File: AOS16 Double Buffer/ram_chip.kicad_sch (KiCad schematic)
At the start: 1 part, among them IC3 IS61WV3216BLL-12TLI

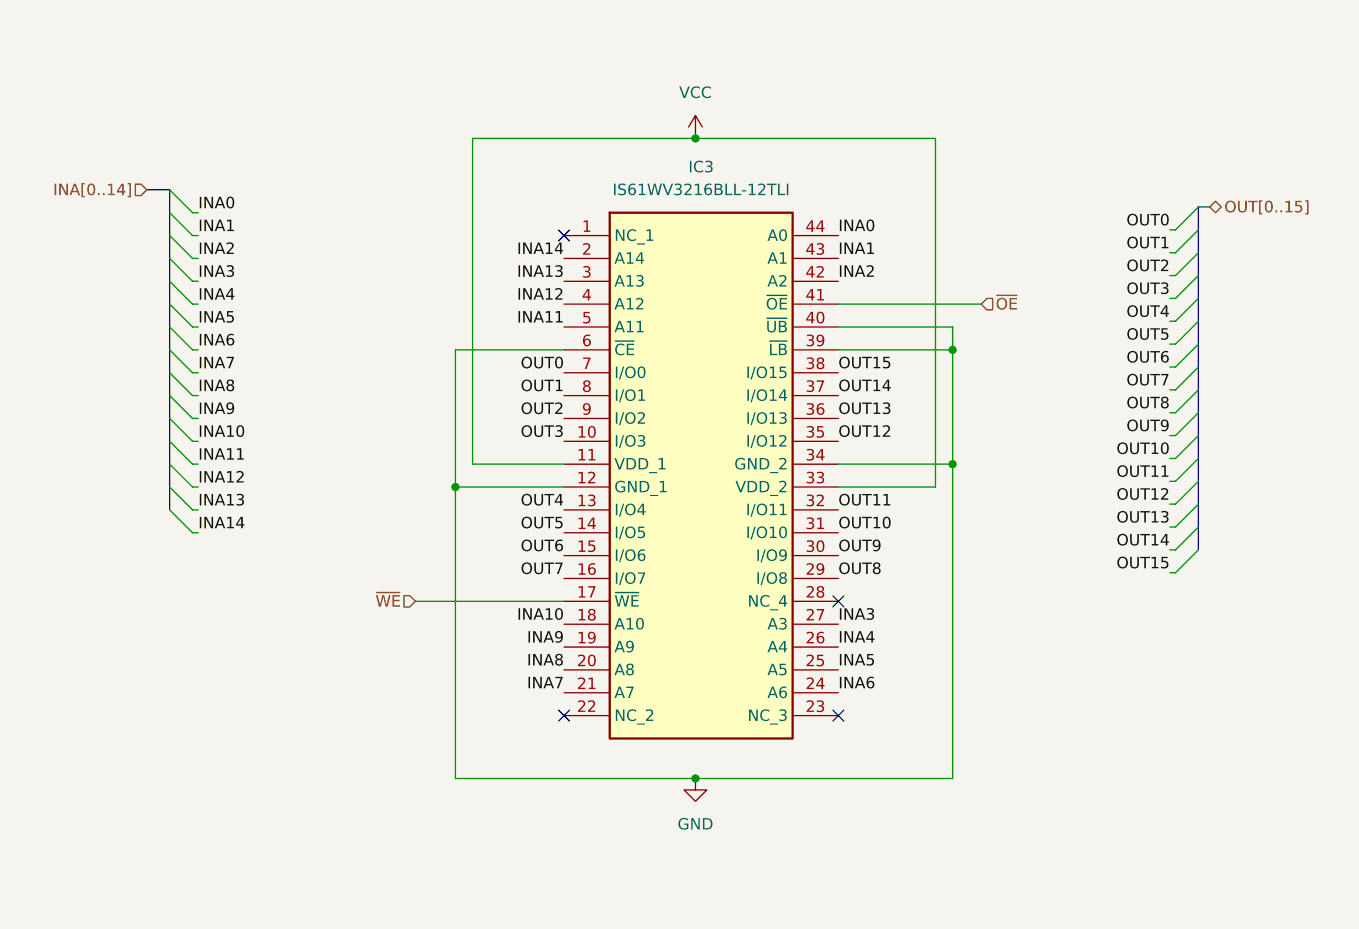
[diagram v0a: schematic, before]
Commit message: updated double buffer
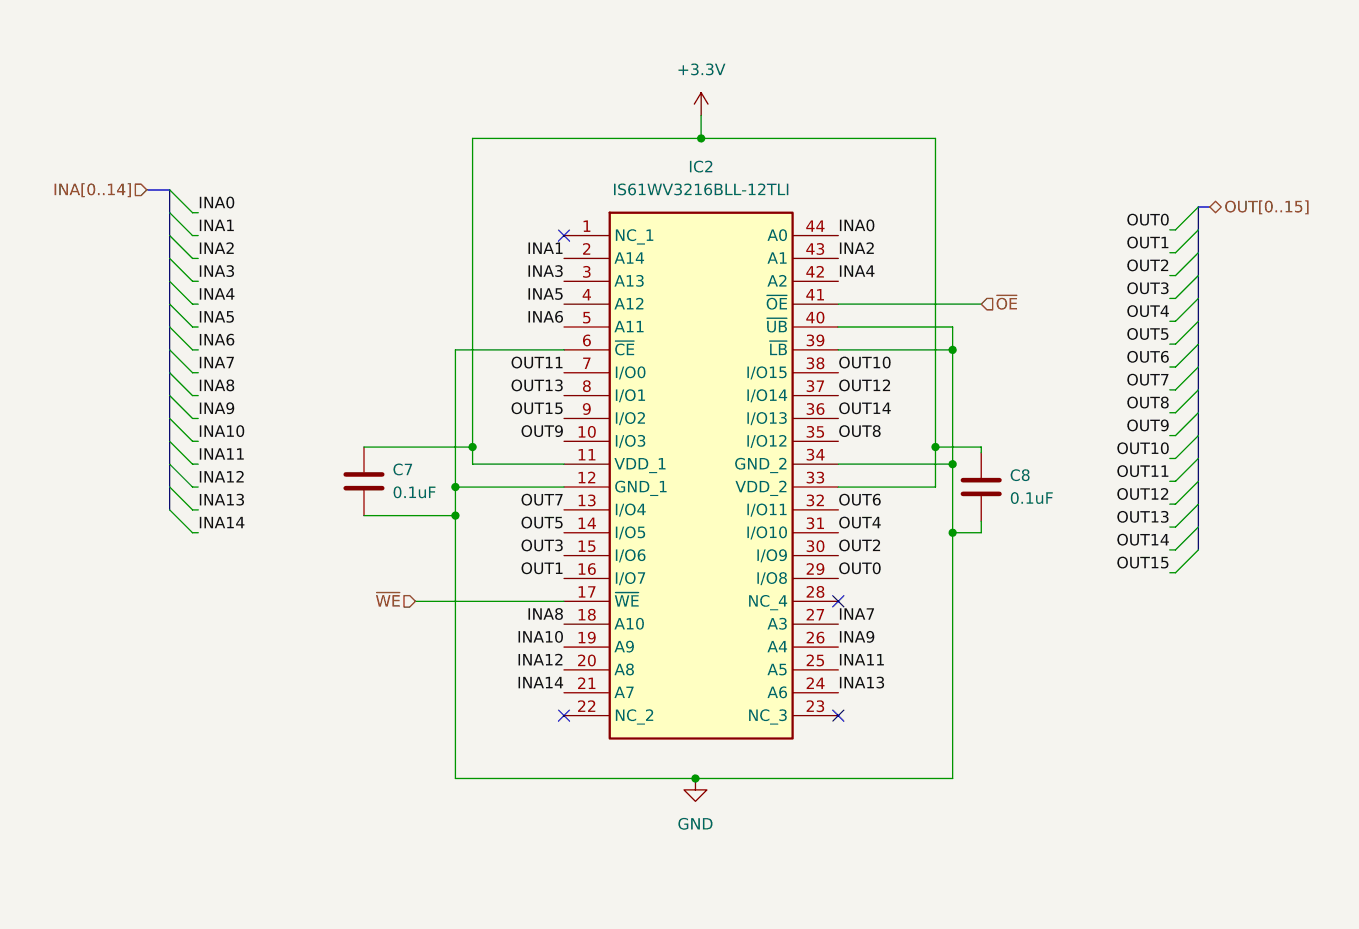
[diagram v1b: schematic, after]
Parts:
- added C7, C8: 0.1uF, Capacitor_SMD:C_0603_1608Metric, symbol Device:C
- renumbered IC3 to IC2
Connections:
- net GND: now also C7.2, C8.2
- net INA1: now also IC2.2 (A14); no longer IC2.43 (A1)
- net INA10: now also IC2.19 (A9); no longer IC2.18 (A10)
- net INA11: now also IC2.25 (A5); no longer IC2.5 (A11)
- net INA12: now also IC2.20 (A8); no longer IC2.4 (A12)
- net INA13: now also IC2.24 (A6); no longer IC2.3 (A13)
- net INA14: now also IC2.21 (A7); no longer IC2.2 (A14)
- net INA2: now also IC2.43 (A1); no longer IC2.42 (A2)
- net INA3: now also IC2.3 (A13); no longer IC2.27 (A3)
- net INA4: now also IC2.42 (A2); no longer IC2.26 (A4)
- net INA5: now also IC2.4 (A12); no longer IC2.25 (A5)
- net INA6: now also IC2.5 (A11); no longer IC2.24 (A6)
- net INA7: now also IC2.27 (A3); no longer IC2.21 (A7)
- net INA8: now also IC2.18 (A10); no longer IC2.20 (A8)
- net INA9: now also IC2.26 (A4); no longer IC2.19 (A9)
- net OUT0: now also IC2.29 (I/O8); no longer IC2.7 (I/O0)
- net OUT1: now also IC2.16 (I/O7); no longer IC2.8 (I/O1)
- net OUT10: now also IC2.38 (I/O15); no longer IC2.31 (I/O10)
- net OUT11: now also IC2.7 (I/O0); no longer IC2.32 (I/O11)
- net OUT12: now also IC2.37 (I/O14); no longer IC2.35 (I/O12)
- net OUT13: now also IC2.8 (I/O1); no longer IC2.36 (I/O13)
- net OUT14: now also IC2.36 (I/O13); no longer IC2.37 (I/O14)
- net OUT15: now also IC2.9 (I/O2); no longer IC2.38 (I/O15)
- net OUT2: now also IC2.30 (I/O9); no longer IC2.9 (I/O2)
- net OUT3: now also IC2.15 (I/O6); no longer IC2.10 (I/O3)
- net OUT4: now also IC2.31 (I/O10); no longer IC2.13 (I/O4)
- net OUT6: now also IC2.32 (I/O11); no longer IC2.15 (I/O6)
- net OUT7: now also IC2.13 (I/O4); no longer IC2.16 (I/O7)
- net OUT8: now also IC2.35 (I/O12); no longer IC2.29 (I/O8)
- net OUT9: now also IC2.10 (I/O3); no longer IC2.30 (I/O9)
- net VCC renamed +3.3V
- net +3.3V: now also C7.1, C8.1

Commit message: Completed double buffer first draft
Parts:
- renumbered C7 to C10, C8 to C11, IC2 to IC1
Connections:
- net OUT0: now also IC1.10 (I/O3); no longer IC1.29 (I/O8)
- net OUT1: now also IC1.36 (I/O13); no longer IC1.16 (I/O7)
- net OUT10: now also IC1.14 (I/O5); no longer IC1.38 (I/O15)
- net OUT11: now also IC1.31 (I/O10); no longer IC1.7 (I/O0)
- net OUT12: now also IC1.15 (I/O6); no longer IC1.37 (I/O14)
- net OUT13: now also IC1.30 (I/O9); no longer IC1.8 (I/O1)
- net OUT14: now also IC1.16 (I/O7); no longer IC1.36 (I/O13)
- net OUT15: now also IC1.29 (I/O8); no longer IC1.9 (I/O2)
- net OUT2: now also IC1.9 (I/O2); no longer IC1.30 (I/O9)
- net OUT3: now also IC1.37 (I/O14); no longer IC1.15 (I/O6)
- net OUT4: now also IC1.8 (I/O1); no longer IC1.31 (I/O10)
- net OUT5: now also IC1.38 (I/O15); no longer IC1.14 (I/O5)
- net OUT6: now also IC1.7 (I/O0); no longer IC1.32 (I/O11)
- net OUT7: now also IC1.35 (I/O12); no longer IC1.13 (I/O4)
- net OUT8: now also IC1.13 (I/O4); no longer IC1.35 (I/O12)
- net OUT9: now also IC1.32 (I/O11); no longer IC1.10 (I/O3)
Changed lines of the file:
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@@
 		)
 	)
-	(label "OUT7"
+	(label "OUT8"
 		(at 105.41 93.345 180)
 		(fields_autoplaced yes)
@@
 		)
 	)
-	(label "OUT2"
+	(label "OUT13"
 		(at 135.89 98.425 0)
 		(fields_autoplaced yes)
@@
 		)
 	)
-	(label "OUT8"
+	(label "OUT7"
 		(at 135.89 85.725 0)
 		(fields_autoplaced yes)
@@
 		)
 	)
-	(label "OUT15"
+	(label "OUT2"
 		(at 105.41 83.185 180)
 		(fields_autoplaced yes)
@@
 		)
 	)
-	(label "OUT12"
+	(label "OUT3"
 		(at 135.89 80.645 0)
 		(fields_autoplaced yes)
@@
 		)
 	)
-	(label "OUT10"
+	(label "OUT5"
 		(at 135.89 78.105 0)
 		(fields_autoplaced yes)
@@
 		)
 	)
+	(label "OUT14"
+		(at 105.41 100.965 180)
+		(fields_autoplaced yes)
+		(effects
+			(font
+				(size 1.27 1.27)
+			)
+			(justify right bottom)
+		)
+	)
 	(label "OUT1"
-		(at 105.41 100.965 180)
-		(fields_autoplaced yes)
-		(effects
-			(font
-				(size 1.27 1.27)
-			)
-			(justify right bottom)
-		)
-	)
-	(label "OUT14"
 		(at 135.89 83.185 0)
 		(fields_autoplaced yes)
@@
 		)
 	)
-	(label "OUT3"
+	(label "OUT12"
 		(at 105.41 98.425 180)
 		(fields_autoplaced yes)
@@
 		)
 	)
-	(label "OUT4"
+	(label "OUT11"
 		(at 135.89 95.885 0)
 		(fields_autoplaced yes)
@@
 		)
 	)
-	(label "OUT13"
+	(label "OUT4"
 		(at 105.41 80.645 180)
 		(fields_autoplaced yes)
@@
 		)
 	)
-	(label "OUT11"
+	(label "OUT6"
 		(at 105.41 78.105 180)
 		(fields_autoplaced yes)
@@
 		)
 	)
-	(label "OUT9"
+	(label "OUT0"
 		(at 105.41 85.725 180)
 		(fields_autoplaced yes)
@@
 		)
 	)
-	(label "OUT6"
+	(label "OUT9"
 		(at 135.89 93.345 0)
 		(fields_autoplaced yes)
@@
 		)
 	)
-	(label "OUT5"
+	(label "OUT10"
 		(at 105.41 95.885 180)
 		(fields_autoplaced yes)
@@
 		)
 	)
-	(label "OUT0"
+	(label "OUT15"
 		(at 135.89 100.965 0)
 		(fields_autoplaced yes)
@@
 		(dnp no)
 		(fields_autoplaced yes)
-		(property "Reference" "IC2"
+		(property "Reference" "IC1"
 			(at 120.65 55.245 0)
 			(effects
@@
 			(project ""
 				(path "/131fc824-3141-4c3d-90f1-eeaffe39dfa6/3f18fc96-0a11-4002-9ee9-db5d8ab4d742"
-					(reference "IC2")
+					(reference "IC1")
 					(unit 1)
 				)
@@
 		(dnp no)
 		(fields_autoplaced yes)
-		(property "Reference" "C7"
+		(property "Reference" "C10"
 			(at 86.36 88.8999 0)
 			(effects
@@
 			(project ""
 				(path "/131fc824-3141-4c3d-90f1-eeaffe39dfa6/3f18fc96-0a11-4002-9ee9-db5d8ab4d742"
-					(reference "C7")
+					(reference "C10")
 					(unit 1)
 				)
@@
 		(dnp no)
 		(fields_autoplaced yes)
-		(property "Reference" "#PWR019"
+		(property "Reference" "#PWR012"
 			(at 120.65 53.34 0)
 			(effects
@@
 			(project ""
 				(path "/131fc824-3141-4c3d-90f1-eeaffe39dfa6/3f18fc96-0a11-4002-9ee9-db5d8ab4d742"
-					(reference "#PWR019")
+					(reference "#PWR012")
 					(unit 1)
 				)
@@
 		(dnp no)
 		(fields_autoplaced yes)
-		(property "Reference" "C8"
+		(property "Reference" "C11"
 			(at 154.94 89.5349 0)
 			(effects
@@
 			(project "AOS16 Double Buffer"
 				(path "/131fc824-3141-4c3d-90f1-eeaffe39dfa6/3f18fc96-0a11-4002-9ee9-db5d8ab4d742"
-					(reference "C8")
+					(reference "C11")
 					(unit 1)
 				)
@@
 		(dnp no)
 		(fields_autoplaced yes)
-		(property "Reference" "#PWR018"
+		(property "Reference" "#PWR011"
 			(at 120.015 129.54 0)
 			(effects
@@
 			(project ""
 				(path "/131fc824-3141-4c3d-90f1-eeaffe39dfa6/3f18fc96-0a11-4002-9ee9-db5d8ab4d742"
-					(reference "#PWR018")
+					(reference "#PWR011")
 					(unit 1)
 				)

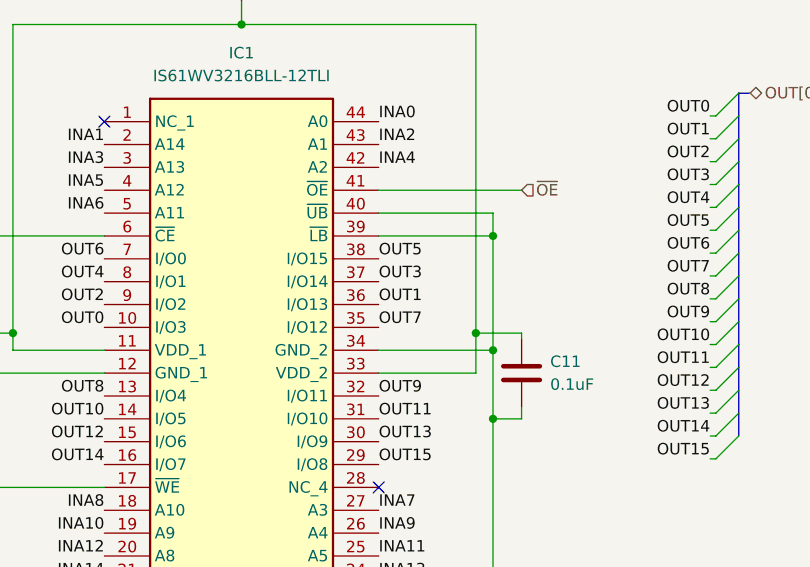
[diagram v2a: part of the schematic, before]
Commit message: Double Buffer Revision
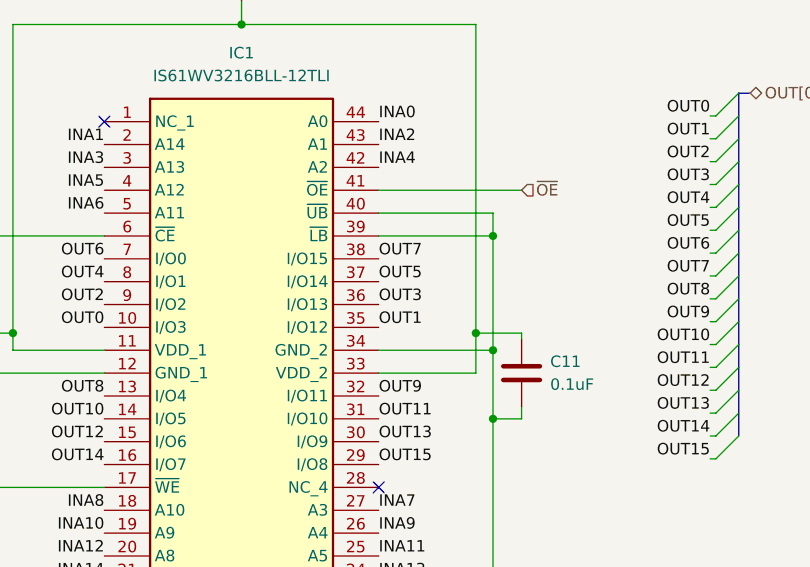
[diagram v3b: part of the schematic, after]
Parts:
- IC1: footprint Package_SO:TSOP-II-44_10.16x18.41mm_P0.8mm -> Package_SO:SOJ-44_10.16x28.575mm_P1.27mm
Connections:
- net OUT1: now also IC1.35 (I/O12); no longer IC1.36 (I/O13)
- net OUT3: now also IC1.36 (I/O13); no longer IC1.37 (I/O14)
- net OUT5: now also IC1.37 (I/O14); no longer IC1.38 (I/O15)
- net OUT7: now also IC1.38 (I/O15); no longer IC1.35 (I/O12)
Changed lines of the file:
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@@
 		)
 	)
-	(label "OUT7"
+	(label "OUT1"
 		(at 135.89 85.725 0)
 		(fields_autoplaced yes)
@@
 		)
 	)
-	(label "OUT3"
+	(label "OUT5"
 		(at 135.89 80.645 0)
 		(fields_autoplaced yes)
@@
 		)
 	)
-	(label "OUT5"
+	(label "OUT7"
 		(at 135.89 78.105 0)
 		(fields_autoplaced yes)
@@
 		)
 	)
-	(label "OUT1"
+	(label "OUT3"
 		(at 135.89 83.185 0)
 		(fields_autoplaced yes)
@@
 			)
 		)
-		(property "Footprint" "Package_SO:TSOP-II-44_10.16x18.41mm_P0.8mm"
+		(property "Footprint" "Package_SO:SOJ-44_10.16x28.575mm_P1.27mm"
 			(at 132.08 157.785 0)
 			(effects

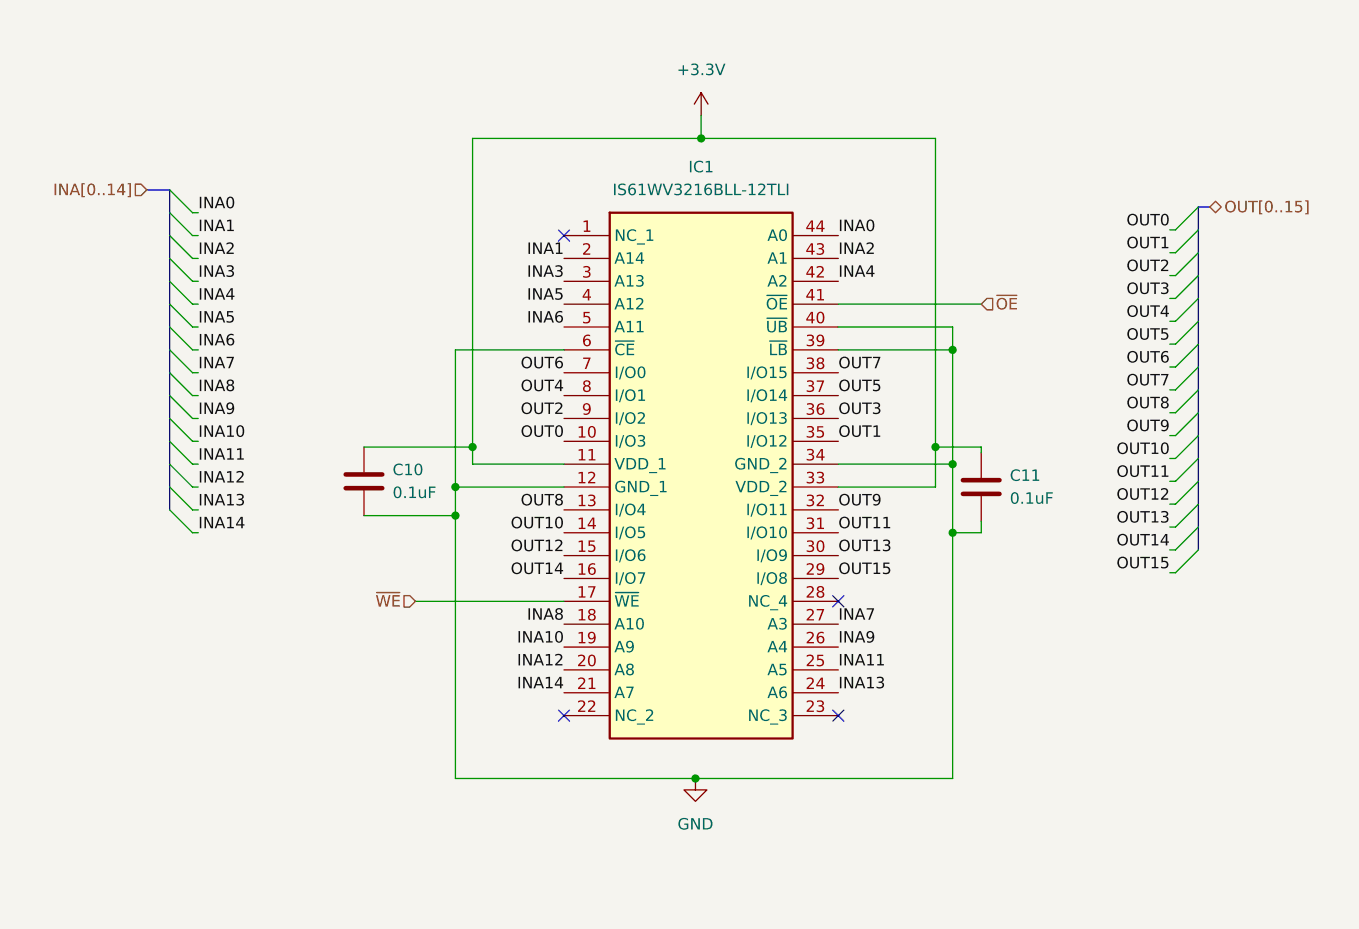
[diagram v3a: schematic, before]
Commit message: Fixed double buffer logic families
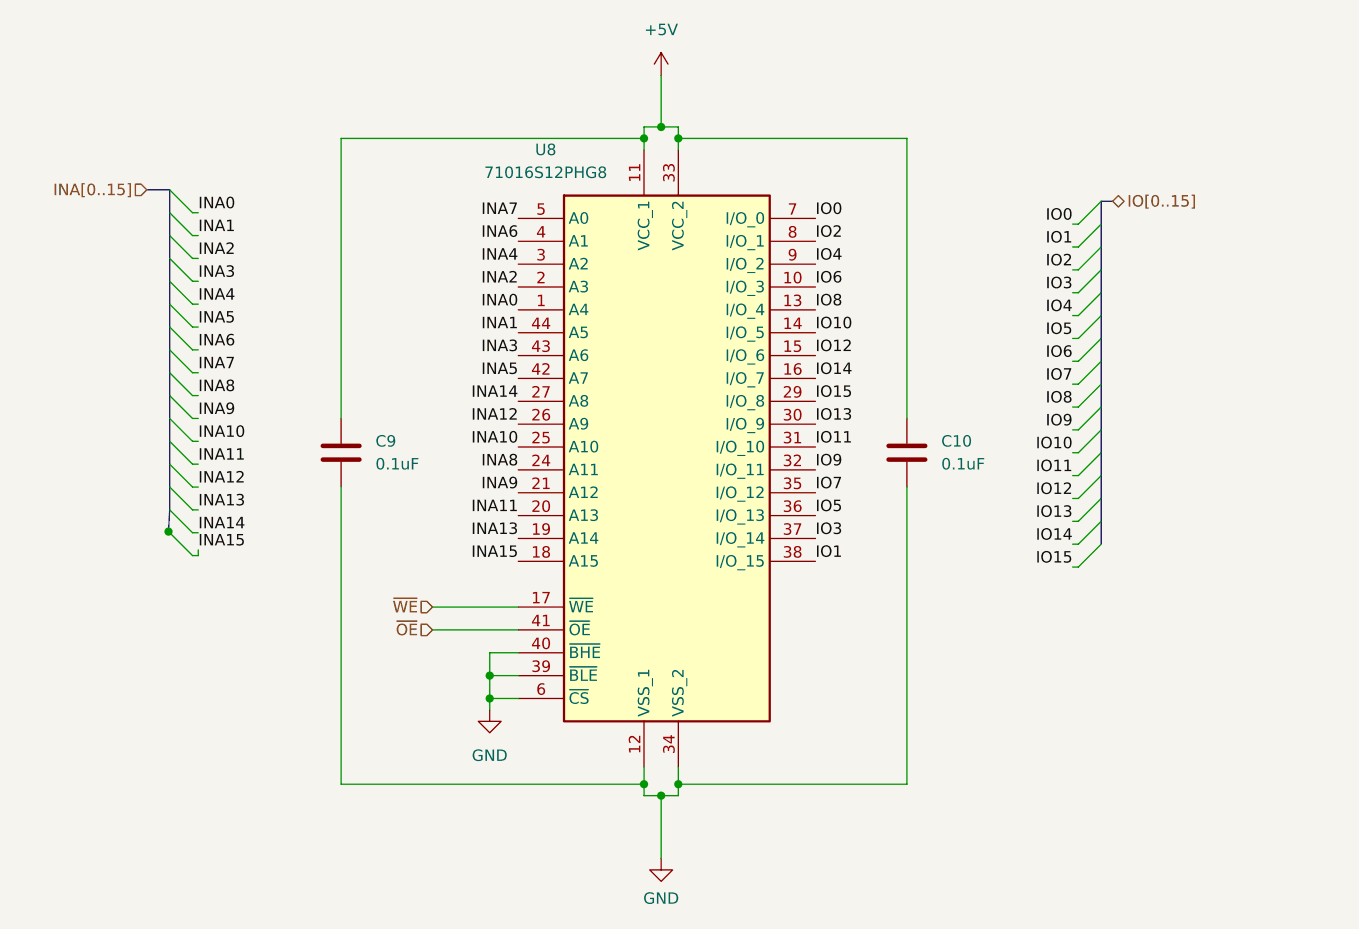
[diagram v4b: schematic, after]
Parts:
- removed C11: 0.1uF, Capacitor_SMD:C_0603_1608Metric, symbol Device:C
- removed IC1: IS61WV3216BLL-12TLI, Package_SO:SOJ-44_10.16x28.575mm_P1.27mm, symbol IS61WV3216BLL-12TLI:IS61WV3216BLL-12TLI
- added C9: 0.1uF, Capacitor_SMD:C_0603_1608Metric, symbol Device:C
- added U8: 71016S12PHG8, Package_SO:TSOP-II-44_10.16x18.41mm_P0.8mm, symbol 71016S12PHG8:71016S12PHG8
- C10: Manufacturer_Part_Number CL10B104KO8WPNL -> (none)
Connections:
- net GND: now also C9.2, U8.12 (VSS_1), U8.34 (VSS_2), U8.39 (~{BLE}), U8.40 (~{BHE}), U8.6 (~{CS})
- net INA0: now also U8.1 (A4)
- net INA1: now also U8.44 (A5)
- net INA10: now also U8.25 (A10)
- net INA11: now also U8.20 (A13)
- net INA12: now also U8.26 (A9)
- net INA13: now also U8.19 (A14)
- net INA14: now also U8.27 (A8)
- net INA2: now also U8.2 (A3)
- net INA3: now also U8.43 (A6)
- net INA4: now also U8.3 (A2)
- net INA5: now also U8.42 (A7)
- net INA6: now also U8.4 (A1)
- net INA7: now also U8.5 (A0)
- net INA8: now also U8.24 (A11)
- net INA9: now also U8.21 (A12)
- net ~{OE}: now also U8.41 (~{OE})
- net ~{WE}: now also U8.17 (~{WE})
- net +3.3V renamed +5V
- net +5V: now also C9.1, U8.11 (VCC_1), U8.33 (VCC_2)
- new net INA15: U8.18 (A15)
- new net IO0: U8.7 (I/O_0)
- new net IO1: U8.38 (I/O_15)
- new net IO10: U8.14 (I/O_5)
- new net IO11: U8.31 (I/O_10)
- new net IO12: U8.15 (I/O_6)
- new net IO13: U8.30 (I/O_9)
- new net IO14: U8.16 (I/O_7)
- new net IO15: U8.29 (I/O_8)
- new net IO2: U8.8 (I/O_1)
- new net IO3: U8.37 (I/O_14)
- new net IO4: U8.9 (I/O_2)
- new net IO5: U8.36 (I/O_13)
- new net IO6: U8.10 (I/O_3)
- new net IO7: U8.35 (I/O_12)
- new net IO8: U8.13 (I/O_4)
- new net IO9: U8.32 (I/O_11)
- no-connect marks 4 -> 0
